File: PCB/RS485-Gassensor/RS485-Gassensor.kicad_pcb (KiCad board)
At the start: 2 copper layers, 18 x 64 mm, 22 parts, among them J1 Conn_01x04, J2 Conn_01x04, U1 STM8S003F3P, U2 MICS-8614, U3 R-785.0-1.0, U4 LT1785xS8, U5 OP179GRT

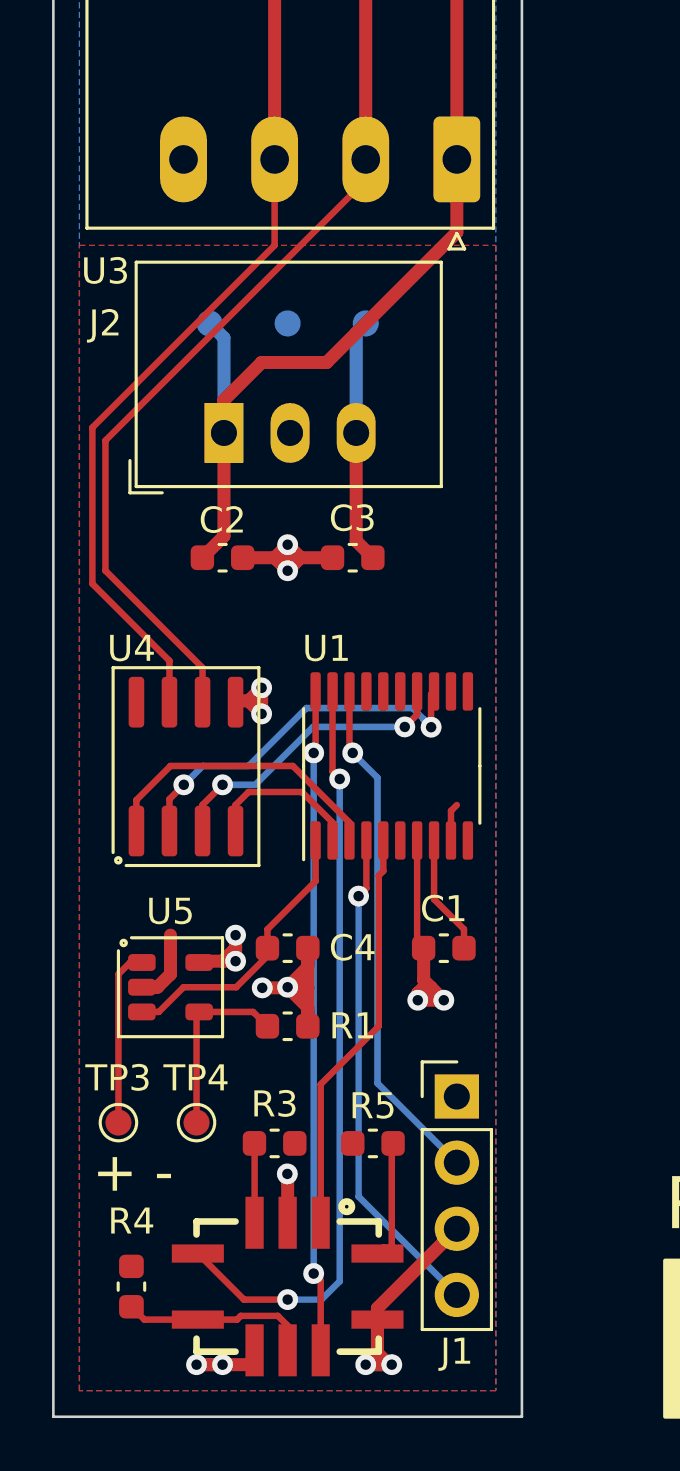
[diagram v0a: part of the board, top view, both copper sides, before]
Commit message: clean up, minor extension
cleaned up /reorganized scematic,
added optional termination resistor for RS-485
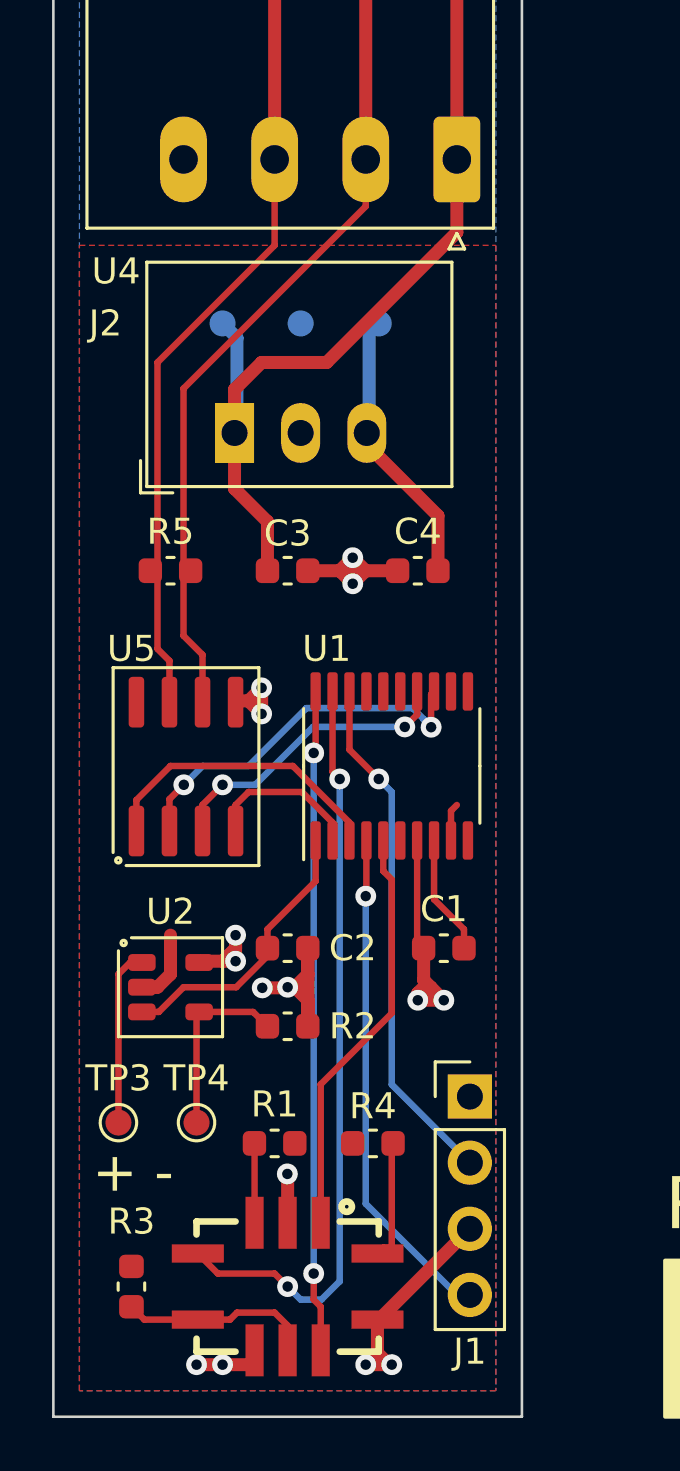
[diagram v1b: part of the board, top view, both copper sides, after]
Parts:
- added R5: R220, Capacitor_SMD:C_0603_1608Metric, F.Cu at (145.5, 56.5)
- moved C3 2.55 mm to (150.0, 56.5)
- moved C4 2.55 mm to (155.0, 56.5)
- moved J1 0.50 mm to (157.0, 76.7)
- moved TP1 0.50 mm to (153.5, 47.0)
- moved TP2 0.50 mm to (150.5, 47.0)
- moved TP5 0.50 mm to (147.5, 47.0)
- moved U4 0.41 mm to (148.0, 51.2)
- renumbered C4 to C2, C2 to C3, C3 to C4, R3 to R1, R1 to R2, R4 to R3, R5 to R4, TP7 to TP5, U5 to U2, U2 to U3, U3 to U4, U4 to U5
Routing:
- net GND: track 46.0 -> 43.4 mm
- net /RS485-A: track 34.7 -> 32.3 mm
- net /RS485-B: track 33.2 -> 31.1 mm
- net +5V: track 13.7 -> 15.0 mm

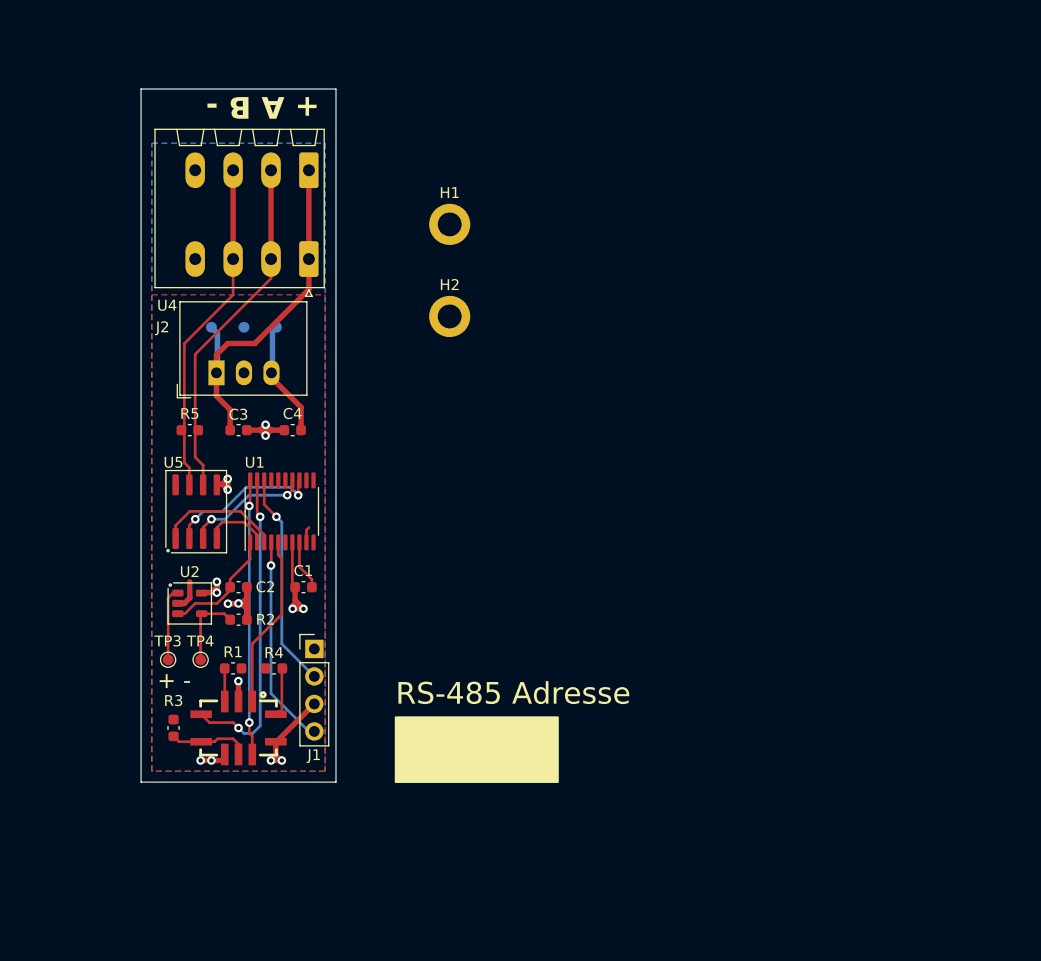
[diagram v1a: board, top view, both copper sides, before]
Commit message: restarted Project.
new PCB, improved component chioce
strarted program with STM32 IDE
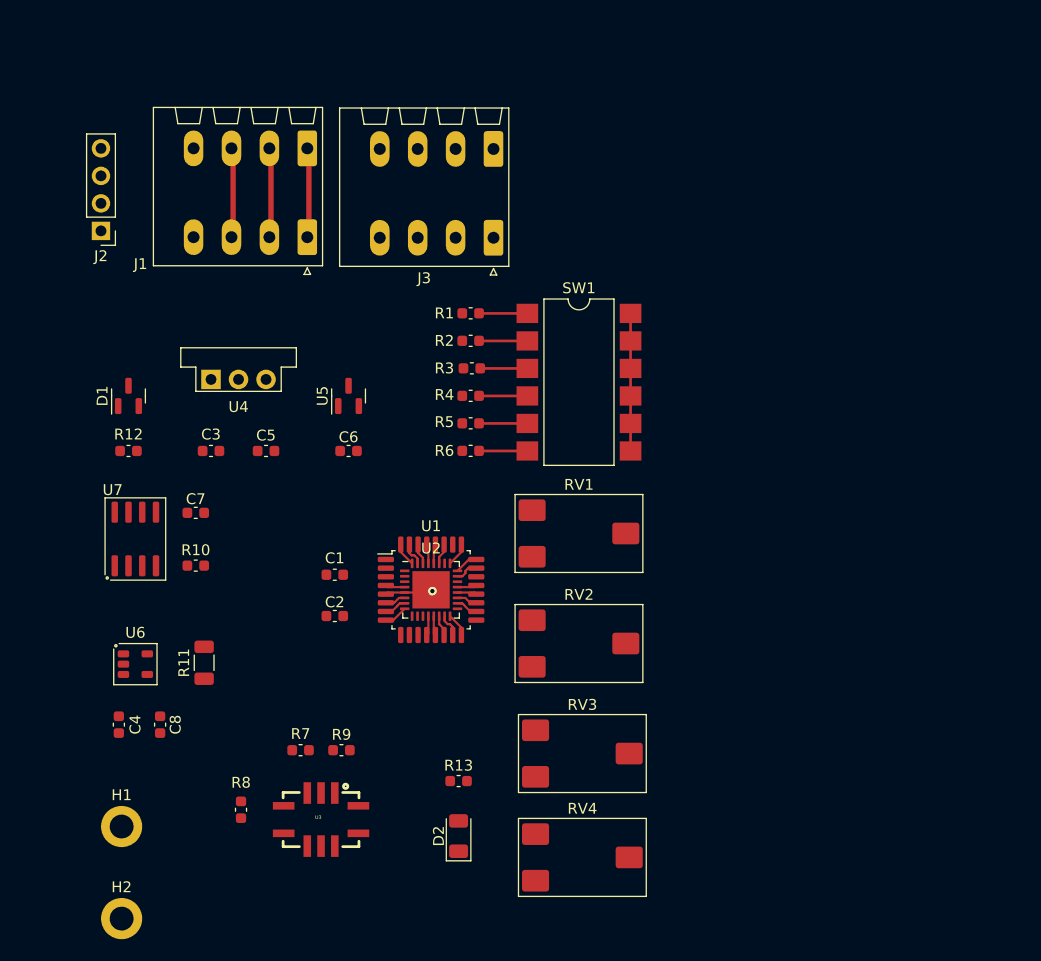
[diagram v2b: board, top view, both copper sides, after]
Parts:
- removed the C1 at (156.0, 71.0)
- removed TP1, TP2, TP3, TP4, TP5: TestPoint, TestPoint:TestPoint_Pad_D1.0mm
- removed the U4 at (148.0, 51.2)
- added C4: CAP4.7uF, Capacitor_SMD:C_0603_1608Metric, F.Cu at (139.0, 83.7)
- added C5: CAP2.2uF, Capacitor_SMD:C_0603_1608Metric, F.Cu at (152.5, 58.4)
- added C6: CAP1uF, Capacitor_SMD:C_0603_1608Metric, F.Cu at (160.2, 58.4)
- added C7: CAP100nF, Capacitor_SMD:C_0603_1608Metric, F.Cu at (146.1, 64.1)
- added C8: CAP100nF, Capacitor_SMD:C_0603_1608Metric, F.Cu at (142.8, 83.7)
- added D1: SM712_SOT23, Package_TO_SOT_SMD:SOT-23, F.Cu at (139.8, 53.3)
- added D2: IR26-21C_L110_TR8, LED_SMD:LED_1206_3216Metric, F.Cu at (170.3, 94.0)
- added J3: Screw_Terminal_01x04, Connector_Phoenix_SPT:PhoenixContact_SPT_1.5_4-H-3.5_1x04_P3.5mm_Horizontal, F.Cu at (173.5, 38.7)
- added R1: R10K, Capacitor_SMD:C_0603_1608Metric, F.Cu at (171.4, 45.7)
- added R10: R10K, Capacitor_SMD:C_0603_1608Metric, F.Cu at (146.1, 69.0)
- added R13: R27, Capacitor_SMD:C_0603_1608Metric, F.Cu at (170.3, 88.9)
- added R2: R10K, Capacitor_SMD:C_0603_1608Metric, F.Cu at (171.4, 48.2)
- added R3: R10K, Capacitor_SMD:C_0603_1608Metric, F.Cu at (171.5, 50.8)
- added R4: R10K, Capacitor_SMD:C_0603_1608Metric, F.Cu at (171.4, 53.3)
- added R5: R10K, Capacitor_SMD:C_0603_1608Metric, F.Cu at (171.4, 55.9)
- added R6: R10K, Capacitor_SMD:C_0603_1608Metric, F.Cu at (171.4, 58.4)
- added RV1: R_Poti, PCM_Potentiometer_SMD_AKL:Potentiometer_ACP_CA6-VSMD_Vertical, F.Cu at (181.4, 66.0)
- added RV2: R_Poti, PCM_Potentiometer_SMD_AKL:Potentiometer_ACP_CA6-VSMD_Vertical, F.Cu at (181.4, 76.2)
- added RV3: R_Poti, PCM_Potentiometer_SMD_AKL:Potentiometer_ACP_CA6-VSMD_Vertical, F.Cu at (181.8, 86.4)
- added RV4: R_Poti, PCM_Potentiometer_SMD_AKL:Potentiometer_ACP_CA6-VSMD_Vertical, F.Cu at (181.8, 96.0)
- added SW1: SW_DIP_x06, Package_DIP:SMDIP-12_W9.53mm, F.Cu at (181.4, 52.1)
- added U2: STM32G031K8Ux, Package_DFN_QFN:QFN-32-1EP_5x5mm_P0.5mm_EP3.45x3.45mm, F.Cu at (167.8, 71.2)
- added U3: MICS-8614, MICS-6814:MICS_8614-SMD, F.Cu at (157.6, 92.5)
- added U5: AP2127N-3.3, Package_TO_SOT_SMD:SOT-23, F.Cu at (160.2, 53.3)
- C1: renamed from C3; value CAP2.2uF -> CAP4.7nF
- C2: value CAP4.7uF -> CAP100nF
- J1: renamed from J2; value Conn_01x04 -> Screw_Terminal_01x04
- J2: renamed from J1; value Conn_01x04 -> Screw_Terminal_01x04
- R11: renamed from R2; value R250 -> R150; footprint Capacitor_SMD:C_0603_1608Metric -> Capacitor_SMD:C_1206_3216Metric
- U1: value STM8S003F3P -> STM32G031K8Tx; footprint Package_SO:TSSOP-20_4.4x6.5mm_P0.65mm -> Package_QFP:LQFP-32_7x7mm_P0.8mm
- U4: renamed from U3; value MICS-8614 -> OKI-78SR-5_1.5-W36-C; footprint MICS-6814:MICS_8614-SMD -> Converter_DCDC:Converter_DCDC_Murata_OKI-78SR_Vertical
- moved H1 63.3 mm to (139.2, 93.1)
- moved H2 63.3 mm to (139.2, 101.6)
- moved J2 43.3 mm to (137.3, 38.1), turned to 180 degrees
- moved U4 32.3 mm to (147.5, 51.8)
- moved C1 16.0 mm to (158.9, 69.8), turned to 180 degrees
- moved U1 15.6 mm to (167.8, 71.2), turned to 0 degrees
- moved R7 9.79 mm to (155.7, 86.0)
- moved R8 9.79 mm to (150.2, 91.5)
- moved R9 9.79 mm to (159.5, 86.0)
- moved C2 9.28 mm to (158.9, 73.7)
- moved C3 7.78 mm to (147.5, 58.4), turned to 0 degrees
- moved U6 7.53 mm to (140.5, 78.1)
- moved U7 6.16 mm to (140.5, 66.5)
- moved R12 5.98 mm to (139.8, 58.4)
- moved R11 5.09 mm to (146.8, 78.0), turned to 90 degrees
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- renumbered C4 to C3, R5 to R12, R1 to R7, R3 to R8, R4 to R9, U2 to U6, U5 to U7
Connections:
- C1 pad 1: +24V -> +5V
- C2 pad 1: /PWM -> +5V
- C3 pad 1: +5V -> +24V
- J2 pad 1: +5V -> +3.3V
- J2 pad 2: /SWIM -> /SWCLK
- J2 pad 4: /NRST -> /SWDIO
- R11 pad 1: /I_Return -> Net-(R11-Pad1)
- R11 pad 2: GND -> /I_Out
- U1 pad 1: /PWM -> unconnected-(U1-PB9-Pad1)
- U1 pad 12: unconnected-(U1-PB4-Pad12) -> /CO
- U1 pad 13: /Read_!Enable -> /NH3
- U1 pad 14: /Write_Enable -> /NO2
- U1 pad 15: /SPI_SCK -> /Gain_NO
- U1 pad 16: /SPI_MOSI -> /offset_NO
- U1 pad 17: /SPI_MISO -> unconnected-(U1-PB2-Pad17)
- U1 pad 18: /SWIM -> /analog_PWM
- U1 pad 19: /NH3 -> /UART_TX
- U1 pad 2: /UATR_TX -> unconnected-(U1-PC14-Pad2)
- U1 pad 20: /CO -> /LED
- U1 pad 3: /UART_RX -> unconnected-(U1-PC15-Pad3)
- U1 pad 4: /NRST -> +5V
- U1 pad 5: /NO2 -> GND
- U1 pad 6: unconnected-(U1-PA2-Pad6) -> /T_NRST-Button
- U1 pad 7: GND -> /Gain_CO
- U1 pad 8: Net-(U1-VCAP) -> /offset_CO
- U1 pad 9: +5V -> unconnected-(U1-PA2-Pad9)
- U6 pad 1: /I_Out -> Net-(R11-Pad1)
- U6 pad 3: /PWM -> /analog_PWM
- U6 pad 4: /I_Return -> /I_Out
- U7 pad 3: /Write_Enable -> /Read_!Enable
- U7 pad 4: /UATR_TX -> /UART_TX
- U7 pad 8: +5V -> +3.3V
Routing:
- net GND: track 43.4 -> 3.99 mm, vias 15 -> 1
- net /NH3: track 29.3 -> 1.80 mm, vias 2 -> 0
- net +24V: track 33.6 -> 8.20 mm
- net /RS485-A: track 32.3 -> 8.20 mm
- net /CO: track 25.5 -> 1.80 mm, vias 2 -> 0
- net /RS485-B: track 31.1 -> 8.20 mm
- net /SWIM: track 20.0 -> 0.00 mm, vias 1 -> 0
- net /NRST: track 18.9 -> 0.00 mm, vias 1 -> 0
- net /NO2: track 16.0 -> 1.92 mm
- net +5V: track 15.0 -> 1.80 mm
- net +3.3V: track 0.00 -> 12.7 mm
- net /Read_!Enable: track 14.5 -> 2.17 mm, vias 2 -> 0
- net /Write_Enable: track 11.6 -> 0.00 mm, vias 2 -> 0
- net /PWM: track 10.9 -> 0.00 mm
- net /UART_RX: track 11.5 -> 1.80 mm
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- removed copper zone on F.Cu, net +5V
- removed copper zone on B.Cu, net GND
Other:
- board outline removed
- board text removed: "+ -"
- board text removed: "+ A B -"
- board text removed: "RS-485 Adresse"

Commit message: new PCB
new PCB, working DMA
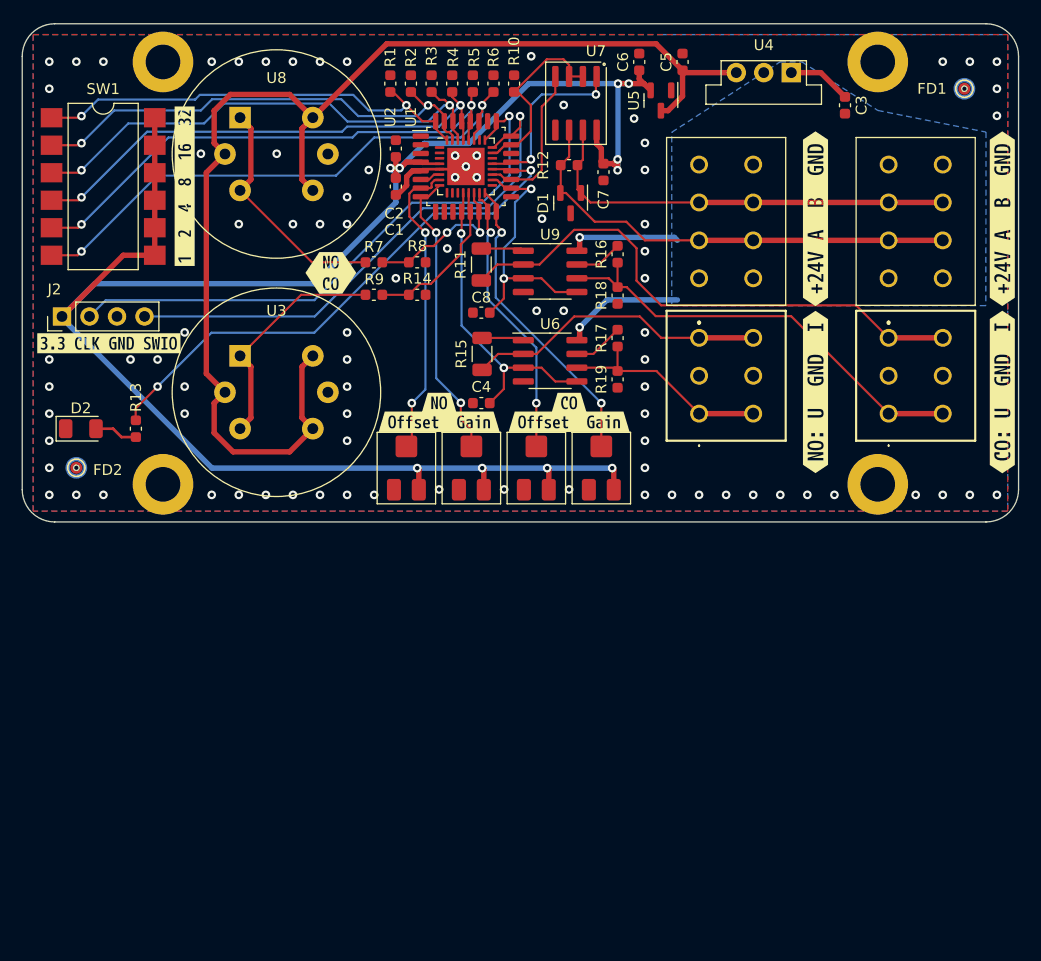
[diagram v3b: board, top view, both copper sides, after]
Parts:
- added FD1: ~, Custom_Library:Alignement_Testpoint_2Layer, F.Cu at (217.0, 25.0)
- added FD2: ~, Custom_Library:Alignement_Testpoint_2Layer, F.Cu at (135.0, 60.0)
- added G***: LOGO, Custom_Library:gas-sensor_ICON, B.Cu at (167.5, 43.5)
- added H3: MountingHole_Pad, MountingHole:MountingHole_3.2mm_M3_DIN965_Pad, F.Cu at (209.0, 61.5)
- added H4: MountingHole_Pad, MountingHole:MountingHole_3.2mm_M3_DIN965_Pad, F.Cu at (143.0, 61.5)
- added J4: Screw_Terminal_01x06, Connector_Phoenix_SPT:1071000, F.Cu at (192.5, 55.0)
- added J5: Screw_Terminal_01x06, Connector_Phoenix_SPT:1071000, F.Cu at (210.0, 55.0)
- added R14: R1K, Capacitor_SMD:C_0603_1608Metric, F.Cu at (166.5, 44.0)
- added R15: R150, Capacitor_SMD:C_1206_3216Metric, F.Cu at (172.5, 49.5)
- added R16: R1K, Capacitor_SMD:C_0603_1608Metric, F.Cu at (185.0, 40.3)
- added R17: R1K, Capacitor_SMD:C_0603_1608Metric, F.Cu at (185.0, 48.0)
- added R18: R1K, Capacitor_SMD:C_0603_1608Metric, F.Cu at (185.0, 44.1)
- added R19: R1K, Capacitor_SMD:C_0603_1608Metric, F.Cu at (185.0, 51.8)
- added U8: MQ-6, Sensor:MQ-6, F.Cu at (150.1, 27.6)
- added U9: AD8676xR, Package_SO:SOIC-8_3.9x4.9mm_P1.27mm, F.Cu at (178.8, 41.8)
- added kibuzzard-64E925B6: G***, kibuzzard-64E925B6, F.Cu at (138.0, 48.5)
- added kibuzzard-64E92756: G***, kibuzzard-64E92756, F.Cu at (145.0, 34.0)
- added kibuzzard-64E927CD: G***, kibuzzard-64E927CD, F.Cu at (158.5, 42.0)
- added kibuzzard-64E9307C: G***, kibuzzard-64E9307C, F.Cu at (203.3, 37.0)
- added kibuzzard-64E9307C: G***, kibuzzard-64E9307C, F.Cu at (220.5, 37.0)
- added kibuzzard-64E930E3: G***, kibuzzard-64E930E3, F.Cu at (220.5, 53.0)
- added kibuzzard-64E93122: G***, kibuzzard-64E93122, F.Cu at (203.3, 53.0)
- added kibuzzard-64E958EB: G***, kibuzzard-64E958EB, F.Cu at (168.5, 54.0)
- added kibuzzard-64E958FD: G***, kibuzzard-64E958FD, F.Cu at (180.5, 54.0)
- added kibuzzard-64E95911: G***, kibuzzard-64E95911, F.Cu at (168.5, 55.7)
- added kibuzzard-64E95911: G***, kibuzzard-64E95911, F.Cu at (180.5, 55.7)
- C4: value CAP4.7uF -> CAP100nF
- H1, H2: footprint MountingHole:MountingHole_2.2mm_M2_DIN965_Pad -> MountingHole:MountingHole_3.2mm_M3_DIN965_Pad
- J1, J3: value Screw_Terminal_01x04 -> Screw_Terminal_01x08; footprint Connector_Phoenix_SPT:PhoenixContact_SPT_1.5_4-H-3.5_1x04_P3.5mm_Horizontal -> Connector_Phoenix_SPT:1862068
- R13: value R27 -> R100
- R7: value R27 -> 470R
- R8: value R820 -> R1K
- R9: value R820 -> 470R
- RV1, RV2, RV3, RV4: value R_Poti -> R_Poti_1K; footprint PCM_Potentiometer_SMD_AKL:Potentiometer_ACP_CA6-VSMD_Vertical -> PCM_Potentiometer_SMD_AKL:Potentiometer_Bourns_3214J_Horizontal
- U3: value MICS-8614 -> MQ-6; footprint MICS-6814:MICS_8614-SMD -> Sensor:MQ-6
- U6: value OP179GRT -> AD8676xR; footprint PCM_Package_TO_SOT_SMD_AKL:SOT-23-5 -> Package_SO:SOIC-8_3.9x4.9mm_P1.27mm
- moved H1 99.3 mm to (209.0, 22.5)
- moved H2 79.2 mm to (143.0, 22.5)
- moved C3 66.7 mm to (206.0, 26.5), turned to -90 degrees
- moved U4 60.6 mm to (201.0, 23.5), turned to 180 degrees
- moved U7 57.2 mm to (181.2, 26.3), turned to -90 degrees
- moved R10 53.3 mm to (175.4, 24.5), turned to 90 degrees
- moved R8 53.1 mm to (166.5, 41.0), turned to 180 degrees
- moved C5 52.6 mm to (191.0, 22.5), turned to 90 degrees
- moved D2 51.3 mm to (135.4, 56.4), turned to 0 degrees
- moved C7 49.1 mm to (183.7, 32.7), turned to -90 degrees
- moved R12 48.5 mm to (180.5, 32.0), turned to 0 degrees
- moved C8 48.2 mm to (172.4, 45.6), turned to 180 degrees
- moved SW1 47.5 mm to (137.5, 34.0)
- moved U6 47.4 mm to (178.8, 50.1)
- moved R7 45.6 mm to (162.5, 41.0), turned to 0 degrees
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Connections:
- C1 pad 1: +5V -> +3.3V
- C2 pad 1: +5V -> +3.3V
- C4 pad 1: /analog_PWM -> /analog_PWM_NO
- C8 pad 1: /analog_PWM -> /analog_PWM_CO
- J1 pad 2: /RS485-A -> +24V
- J1 pad 3: /RS485-B -> /RS485-A
- J1 pad 4: GND -> /RS485-A
- J3 pad 2: /RS485-A -> +24V
- J3 pad 3: /RS485-B -> /RS485-A
- J3 pad 4: GND -> /RS485-A
- R11 pad 2: /I_Out -> /I_Out_CO
- R7 pad 1: +5V -> Net-(U8-B1)
- R7 pad 2: Net-(U3-RH1_NH3) -> /NO2
- R8 pad 1: +5V -> GND
- R8 pad 2: Net-(U3-RH2_RED) -> /NO2
- R9 pad 1: +5V -> Net-(U3-B1)
- R9 pad 2: Net-(U3-RH2_OX) -> /CO
- RV2 pad 2: /Gain_NO -> /offset_CO
- RV3 pad 2: /offset_CO -> /Gain_NO
- U1 pad 12: /CO -> /analog_PWM_NO
- U1 pad 13: /NH3 -> /CO
- U1 pad 18: /analog_PWM -> /analog_PWM_CO
- U1 pad 4: +5V -> +3.3V
- U2 pad 12: /CO -> /analog_PWM_NO
- U2 pad 13: /NH3 -> /CO
- U2 pad 18: /analog_PWM -> /analog_PWM_CO
- U2 pad 4: +5V -> +3.3V
- U6 pad 1: Net-(R11-Pad1) -> Net-(R15-Pad1)
- U6 pad 2: +5V -> /I_Out_NO
- U6 pad 3: /analog_PWM -> /analog_PWM_NO
- U6 pad 4: /I_Out -> GND
- U6 pad 5: GND -> /analog_PWM_NO
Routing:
- net +3.3V: track 12.7 -> 178.1 mm, vias 0 -> 10
- net +5V: track 1.80 -> 116.4 mm
- net /SWCLK: track 2.17 -> 53.2 mm, vias 0 -> 1
- net /I_Out_CO: track 0.00 -> 50.4 mm
- net /LED: track 1.80 -> 50.6 mm, vias 0 -> 2
- net /SWDIO: track 2.17 -> 49.9 mm, vias 0 -> 1
- net /DIP5: track 6.39 -> 51.3 mm, vias 0 -> 2
- net /DIP4: track 6.26 -> 48.3 mm, vias 0 -> 2
- net /U_Out_CO: track 0.00 -> 41.2 mm
- net /DIP3: track 6.26 -> 46.4 mm, vias 0 -> 2
- net /DIP2: track 6.28 -> 46.4 mm, vias 0 -> 2
- net /DIP1: track 6.66 -> 44.3 mm, vias 0 -> 2
- net /DIP0: track 6.64 -> 41.9 mm, vias 0 -> 2
- net /RS485-A: track 8.20 -> 43.3 mm
- net /RS485-B: track 8.20 -> 39.9 mm
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- added copper zone on B.Cu, net +24V
- added copper zone on B.Cu, net GND
- added copper zone on F.Cu, net GND
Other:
- board outline added: 92 x 46 mm
- board text added: "PROTOTYPE V1 Garage Gas Sensor Felix Sarbach 2023"
